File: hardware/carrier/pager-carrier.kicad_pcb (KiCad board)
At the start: 2 copper layers, 85 x 52 mm, 109 parts, among them J1 USB4235, J2 BATTERY, J3 PANEL, J4 CARDKB, J6 MSG_LED, J7 HAPTIC, M1 Walter, Q1 DMG2305UX-7, Q2 UMH3N, Q4 2N7002, SW1 JS102011SAQN, SW2 SKQGAFE010, U1 BQ25185DLHR, U10 MAX17048G+T10, U3 TPS62840DLCR, U4 TPS22917DBV, U5 CP2102N-A02-GQFN24, U6 SN74LVC2G126DCUR, U7 LIS2DW12TR, U9 DRV2605LDGSR

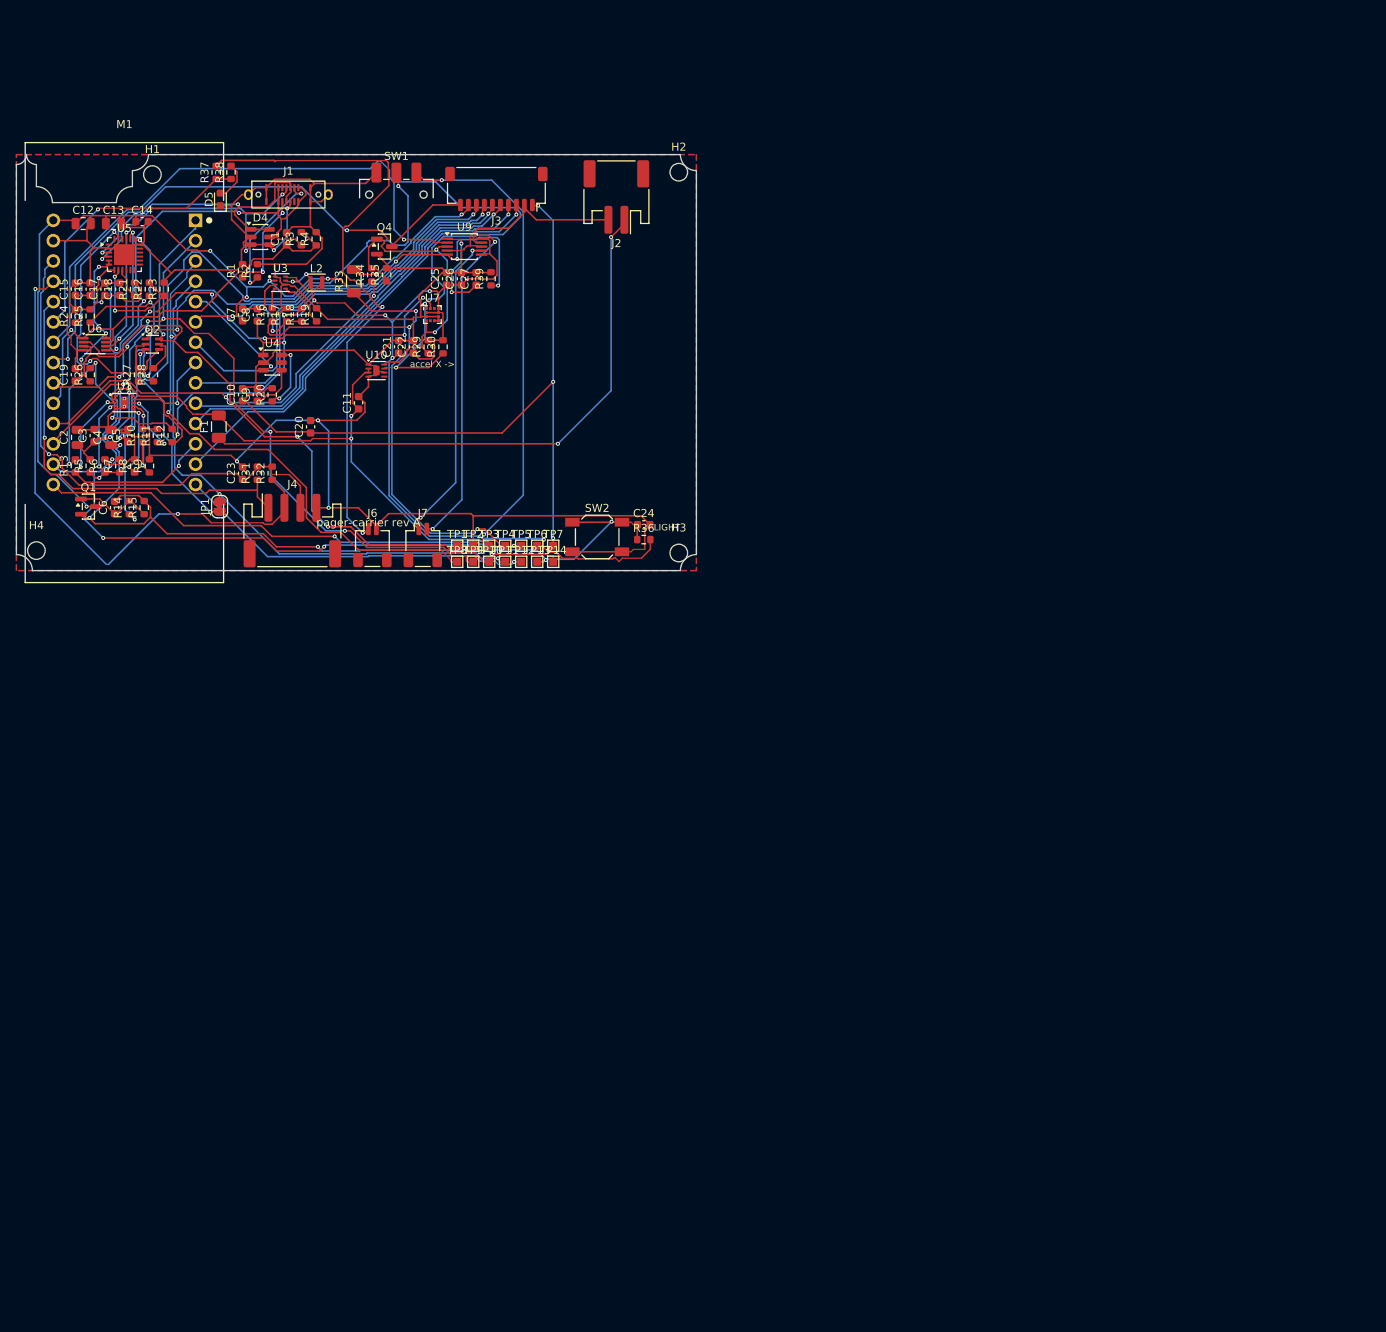
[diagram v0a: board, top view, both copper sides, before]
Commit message: Move sheets property to top level
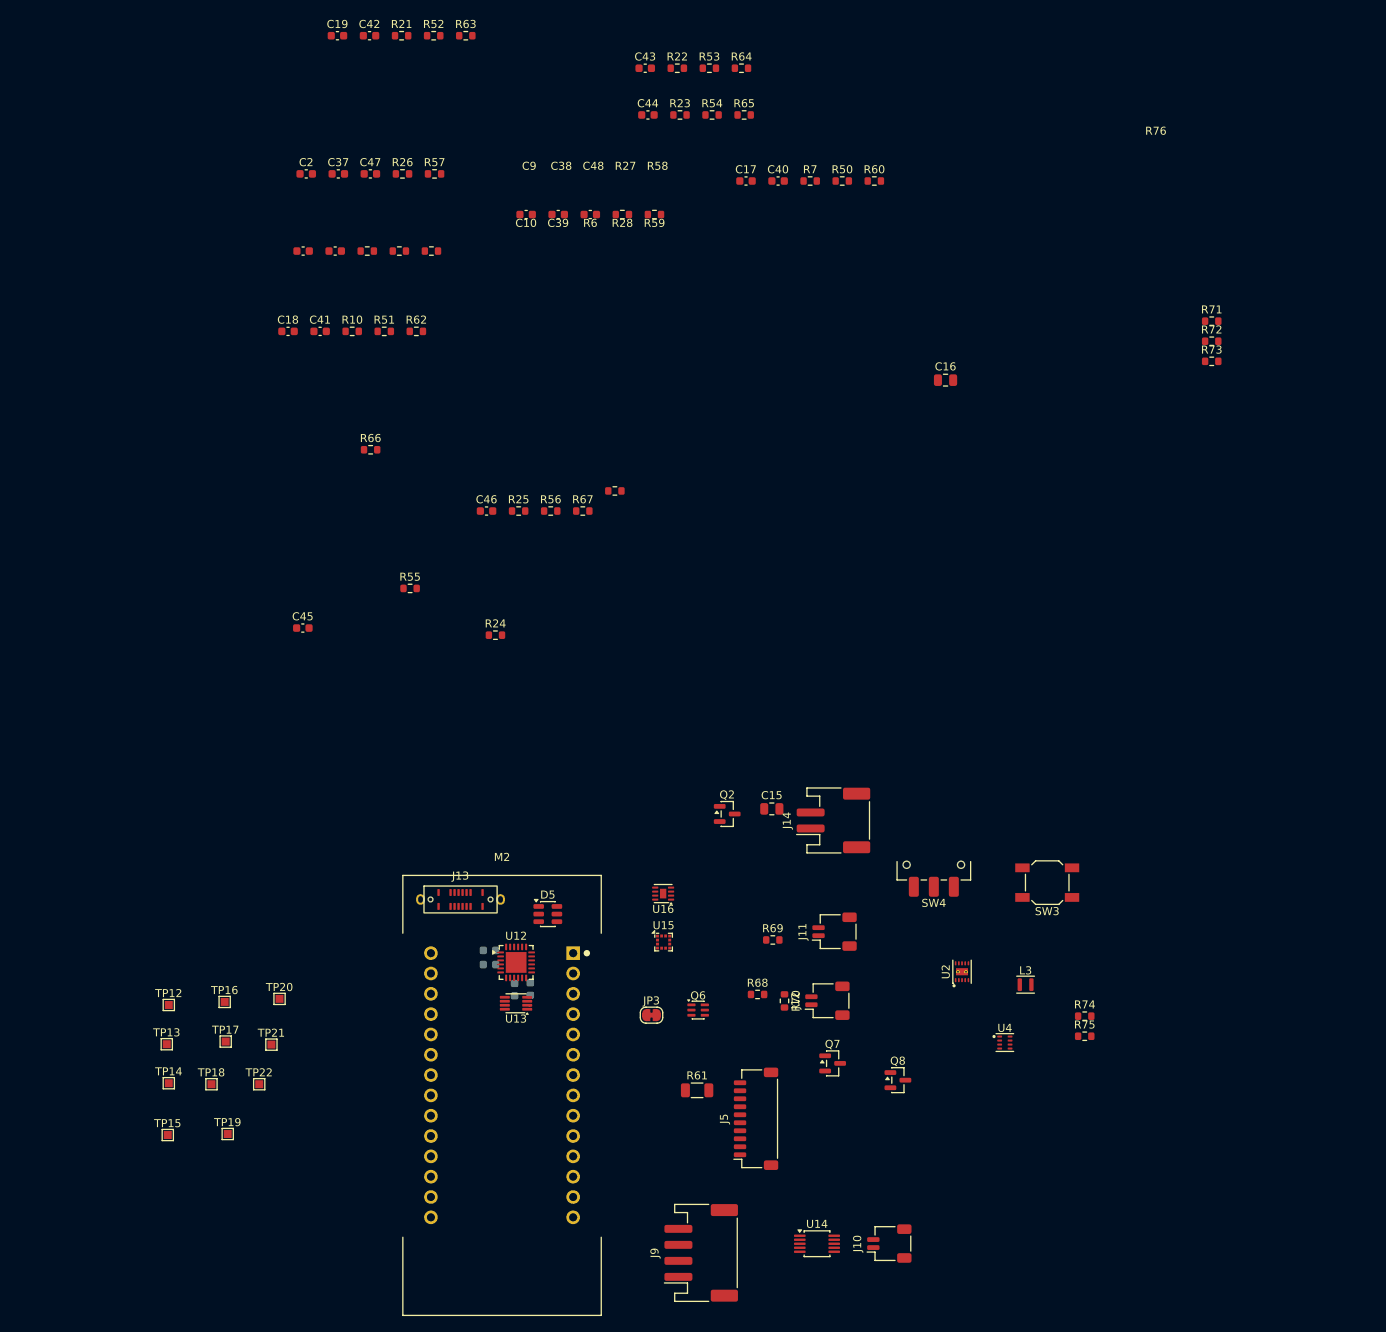
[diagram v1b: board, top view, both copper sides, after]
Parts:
- removed C1, C11, C21, C24, C26: 100nF, Capacitor_SMD:C_0603_1608Metric
- removed C12, C13: 100uF, Capacitor_SMD:C_0805_2012Metric
- removed C14, C20, C22, C23, C5, C7, C8: 10uF, Capacitor_SMD:C_0603_1608Metric
- removed C25, C27: 1uF, Capacitor_SMD:C_0603_1608Metric
- removed C3: 1uF/25V, Capacitor_SMD:C_0603_1608Metric
- removed C4: 22uF, Capacitor_SMD:C_0805_2012Metric
- removed C6: 22nF, Capacitor_SMD:C_0603_1608Metric
- removed D4: USBLC6-2SC6, Package_TO_SOT_SMD:SOT-23-6
- removed F1: 2A PTC, Fuse:Fuse_1206_3216Metric
- removed H1, H2, H3, H4: M2, MountingHole:MountingHole_2.2mm_M2
- removed J1: USB4235, pager-carrier:USB_C_Receptacle_GCT_USB4235_Vertical
- removed J2: BATTERY, Connector_JST:JST_PH_S2B-PH-SM4-TB_1x02-1MP_P2.00mm_Horizontal
- removed J3: PANEL, Connector_JST:JST_SH_SM10B-SRSS-TB_1x10-1MP_P1.00mm_Horizontal
- removed J4: CARDKB, Connector_JST:JST_PH_S4B-PH-SM4-TB_1x04-1MP_P2.00mm_Horizontal
- removed J6: MSG_LED, Connector_JST:JST_SH_SM02B-SRSS-TB_1x02-1MP_P1.00mm_Horizontal
- removed J7: HAPTIC, Connector_JST:JST_SH_SM02B-SRSS-TB_1x02-1MP_P1.00mm_Horizontal
- removed JP1: auto-boot, Jumper:SolderJumper-2_P1.3mm_Bridged_RoundedPad1.0x1.5mm
- removed L2: 2.2uH, Inductor_SMD:L_Murata_DFE201610P
- removed M1: Walter, pager-carrier:Walter_Module_2x14_THT
- removed Q1: DMG2305UX-7, Package_TO_SOT_SMD:SOT-23
- removed Q4: 2N7002, Package_TO_SOT_SMD:SOT-23
- removed R1, R2: 5.1k, Resistor_SMD:R_0603_1608Metric
- removed R11: 604R, Resistor_SMD:R_0603_1608Metric
- removed R12, R13, R14, R8: 10k, Resistor_SMD:R_0603_1608Metric
- removed R15: 2.2M, Resistor_SMD:R_0603_1608Metric
- removed R16, R35, R36, R39, R4: 100k, Resistor_SMD:R_0603_1608Metric
- removed R17, R18, R20, R5: 0R, Resistor_SMD:R_0603_1608Metric
- removed R19: 267k, Resistor_SMD:R_0603_1608Metric
- removed R29, R30, R31, R32: 4.7k, Resistor_SMD:R_0603_1608Metric
- removed R3: 56k, Resistor_SMD:R_0603_1608Metric
- removed R33: 33R, Resistor_SMD:R_1206_3216Metric
- removed R34: 100R, Resistor_SMD:R_0603_1608Metric
- removed R37: 330R, Resistor_SMD:R_0603_1608Metric
- removed R38: 1k, Resistor_SMD:R_0603_1608Metric
- removed R9: 18k, Resistor_SMD:R_0603_1608Metric
- removed SW1: JS102011SAQN, Button_Switch_SMD:SW_SPDT_CK_JS102011SAQN
- removed SW2: SKQGAFE010, Button_Switch_SMD:SW_SPST_SKQG_WithoutStem
- removed TP1, TP2: GND, TestPoint:TestPoint_Pad_1.0x1.0mm
- removed TP10: ESP_EN, TestPoint:TestPoint_Pad_1.0x1.0mm
- removed TP11: KBD_PWR_N, TestPoint:TestPoint_Pad_1.0x1.0mm
- removed TP3: SYS, TestPoint:TestPoint_Pad_1.0x1.0mm
- removed TP4: SYS_SW, TestPoint:TestPoint_Pad_1.0x1.0mm
- removed TP5: VBAT, TestPoint:TestPoint_Pad_1.0x1.0mm
- removed TP6: 3V3, TestPoint:TestPoint_Pad_1.0x1.0mm
- removed TP7: 3V3_EPD, TestPoint:TestPoint_Pad_1.0x1.0mm
- removed TP8: ESP_TX0, TestPoint:TestPoint_Pad_1.0x1.0mm
- removed TP9: ESP_RX0, TestPoint:TestPoint_Pad_1.0x1.0mm
- removed U1: BQ25185DLHR, pager-carrier:BQ25185_WSON-10_DLH0010A_2.2x2mm_P0.4mm_EP0.9x1.5mm
- removed U10: MAX17048G+T10, Package_DFN_QFN:TDFN-8-1EP_2x2mm_P0.5mm_EP0.8x1.2mm
- removed U3: TPS62840DLCR, pager-carrier:TPS62840_VSON-HR-8_DLC0008B_1.5x2mm_P0.5mm
- removed U5: CP2102N-A02-GQFN24, Package_DFN_QFN:QFN-24-1EP_4x4mm_P0.5mm_EP2.6x2.6mm
- removed U6: SN74LVC2G126DCUR, Package_SO:VSSOP-8_2.3x2mm_P0.5mm
- removed U7: LIS2DW12TR, Package_LGA:LGA-12_2x2mm_P0.5mm
- removed U9: DRV2605LDGSR, Package_SO:TSSOP-10_3x3mm_P0.5mm
- added C33: 4.7uF, Capacitor_SMD:C_0603_1608Metric, B.Cu at (59.1, 99.5)
- added C34: 100nF, Capacitor_SMD:C_0603_1608Metric, B.Cu at (59.1, 101.2)
- added C35: 100nF, Capacitor_SMD:C_0603_1608Metric, B.Cu at (62.3, 104.4)
- added C36: 4.7uF, Capacitor_SMD:C_0603_1608Metric, B.Cu at (64.2, 104.3)
- added C37: 100nF, Capacitor_SMD:C_0603_1608Metric, F.Cu at (40.2, 2.41)
- added C38: 10uF, Capacitor_SMD:C_0603_1608Metric, F.Cu at (67.7, 7.49)
- added C39: 100nF, Capacitor_SMD:C_0603_1608Metric, F.Cu at (39.9, 12.1)
- added C40: 10uF, Capacitor_SMD:C_0603_1608Metric, F.Cu at (95.2, 3.30)
- added C41: 1uF, Capacitor_SMD:C_0603_1608Metric, F.Cu at (38.0, 22.1)
- added C42: 100nF, Capacitor_SMD:C_0603_1608Metric, F.Cu at (44.1, -14.9)
- added C43: 10uF, Capacitor_SMD:C_0603_1608Metric, F.Cu at (78.6, -10.8)
- added C44: 1uF, Capacitor_SMD:C_0603_1608Metric, F.Cu at (78.9, -4.95)
- added C45: 100nF, Capacitor_SMD:C_0603_1608Metric, F.Cu at (35.8, 59.2)
- added C46: 100nF, Capacitor_SMD:C_0603_1608Metric, F.Cu at (58.8, 44.6)
- added C47: 10uF, Capacitor_SMD:C_0603_1608Metric, F.Cu at (44.2, 2.41)
- added C48: 10uF, Capacitor_SMD:C_0603_1608Metric, F.Cu at (71.7, 7.49)
- added J10: HAPTIC, Connector_JST:JST_SH_SM02B-SRSS-TB_1x02-1MP_P1.00mm_Horizontal, F.Cu at (109.1, 136.1)
- added J11: EXT_LED, Connector_JST:JST_SH_SM02B-SRSS-TB_1x02-1MP_P1.00mm_Horizontal, F.Cu at (102.3, 97.1)
- added J12: PIEZ, Connector_JST:JST_SH_SM02B-SRSS-TB_1x02-1MP_P1.00mm_Horizontal, F.Cu at (101.4, 105.8)
- added J13: USB4235, pager-carrier:USB_C_Receptacle_GCT_USB4235_Vertical, F.Cu at (55.5, 93.1)
- added J14: BATTERY, Connector_JST:JST_PH_S2B-PH-SM4-TB_1x02-1MP_P2.00mm_Horizontal, F.Cu at (102.1, 83.2)
- added J5: PANEL, Connector_JST:JST_SH_SM10B-SRSS-TB_1x10-1MP_P1.00mm_Horizontal, F.Cu at (92.5, 120.5)
- added J9: CARDKB, Connector_JST:JST_PH_S4B-PH-SM4-TB_1x04-1MP_P2.00mm_Horizontal, F.Cu at (85.6, 137.3)
- added JP3: auto-boot, Jumper:SolderJumper-2_P1.3mm_Bridged_RoundedPad1.0x1.5mm, F.Cu at (79.4, 107.6)
- added L3: 2.2uH, Inductor_SMD:L_Murata_DFE201610P, F.Cu at (126.1, 103.8)
- added M2: Walter, pager-carrier:Walter_Module_2x14_THT, F.Cu at (60.7, 116.3)
- added Q6: UMH3N, Package_TO_SOT_SMD:SOT-363_SC-70-6, F.Cu at (85.2, 106.9)
- added Q7: AO3400A, Package_TO_SOT_SMD:SOT-23, F.Cu at (102.0, 113.6)
- added Q8: MMBT3904, Package_TO_SOT_SMD:SOT-23, F.Cu at (110.2, 115.7)
- added R50: 22.1k, Resistor_SMD:R_0603_1608Metric, F.Cu at (103.2, 3.30)
- added R51: 47.5k, Resistor_SMD:R_0603_1608Metric, F.Cu at (46.0, 22.1)
- added R52: 1k, Resistor_SMD:R_0603_1608Metric, F.Cu at (52.2, -14.9)
- added R53: 100k, Resistor_SMD:R_0603_1608Metric, F.Cu at (86.6, -10.8)
- added R54: 100k, Resistor_SMD:R_0603_1608Metric, F.Cu at (87.0, -4.95)
- added R55: 100k, Resistor_SMD:R_0603_1608Metric, F.Cu at (49.2, 54.2)
- added R56: 10k, Resistor_SMD:R_0603_1608Metric, F.Cu at (66.8, 44.6)
- added R57: 10k, Resistor_SMD:R_0603_1608Metric, F.Cu at (52.3, 2.41)
- added R58: 1k, Resistor_SMD:R_0603_1608Metric, F.Cu at (79.8, 7.49)
- added R59: 100k, Resistor_SMD:R_0603_1608Metric, F.Cu at (51.9, 12.1)
- added R60: 15R, Resistor_SMD:R_0603_1608Metric, F.Cu at (107.2, 3.30)
- added R61: 0R, Resistor_SMD:R_1206_3216Metric, F.Cu at (85.1, 117.0)
- added R62: 10k, Resistor_SMD:R_0603_1608Metric, F.Cu at (50.0, 22.1)
- added R63: 4.7k, Resistor_SMD:R_0603_1608Metric, F.Cu at (56.2, -14.9)
- added R64: 4.7k, Resistor_SMD:R_0603_1608Metric, F.Cu at (90.6, -10.8)
- added R65: 4.7k, Resistor_SMD:R_0603_1608Metric, F.Cu at (91.0, -4.95)
- added R66: 4.7k, Resistor_SMD:R_0603_1608Metric, F.Cu at (44.3, 36.9)
- added R67: 220R, Resistor_SMD:R_0603_1608Metric, F.Cu at (70.8, 44.6)
- added R68: 220R, Resistor_SMD:R_0603_1608Metric, F.Cu at (92.6, 105.0)
- added R69: 330R, Resistor_SMD:R_0603_1608Metric, F.Cu at (94.6, 98.2)
- added R70: 1M, Resistor_SMD:R_0603_1608Metric, F.Cu at (96.0, 105.8)
- added R71: 56k, Resistor_SMD:R_0603_1608Metric, F.Cu at (149.4, 20.8)
- added R72: 100k, Resistor_SMD:R_0603_1608Metric, F.Cu at (149.4, 23.3)
- added R73: 0R, Resistor_SMD:R_0603_1608Metric, F.Cu at (149.4, 25.8)
- added R74: 0R, Resistor_SMD:R_0603_1608Metric, F.Cu at (133.5, 107.7)
- added R75: 100k, Resistor_SMD:R_0603_1608Metric, F.Cu at (133.5, 110.2)
- added R76: 267k, Resistor_SMD:R_0603_1608Metric, F.Cu at (74.8, 42.0)
- added SW3: SKQGAFE010, Button_Switch_SMD:SW_SPST_SKQG_WithoutStem, F.Cu at (128.9, 91.0)
- added SW4: JS102011SAQN, Button_Switch_SMD:SW_SPDT_CK_JS102011SAQN, F.Cu at (114.7, 88.8)
- added TP15: FL_BTN, TestPoint:TestPoint_Pad_1.0x1.0mm, F.Cu at (18.9, 122.6)
- added TP16: 3V3_AWK, TestPoint:TestPoint_Pad_1.0x1.0mm, F.Cu at (26.0, 105.9)
- added TP17: GND, TestPoint:TestPoint_Pad_1.0x1.0mm, F.Cu at (26.2, 110.9)
- added TP18: VBUS, TestPoint:TestPoint_Pad_1.0x1.0mm, F.Cu at (24.4, 116.2)
- added TP19: SYS, TestPoint:TestPoint_Pad_1.0x1.0mm, F.Cu at (26.4, 122.4)
- added TP20: SYS_SW, TestPoint:TestPoint_Pad_1.0x1.0mm, F.Cu at (32.9, 105.5)
- added TP21: VBAT, TestPoint:TestPoint_Pad_1.0x1.0mm, F.Cu at (31.9, 111.3)
- added TP22: 3V3, TestPoint:TestPoint_Pad_1.0x1.0mm, F.Cu at (30.4, 116.2)
- added U12: CP2102N-A02-GQFN24, Package_DFN_QFN:QFN-24-1EP_4x4mm_P0.5mm_EP2.6x2.6mm, F.Cu at (62.5, 101.0)
- added U13: SN74LVC2G126DCUR, Package_SO:VSSOP-8_2.3x2mm_P0.5mm, F.Cu at (62.5, 106.1)
- added U14: DRV2605LDGSR, Package_SO:TSSOP-10_3x3mm_P0.5mm, F.Cu at (100.1, 136.1)
- added U15: LIS2DW12TR, Package_LGA:LGA-12_2x2mm_P0.5mm, F.Cu at (80.9, 98.4)
- added U16: MAX17048G+T10, Package_DFN_QFN:TDFN-8-1EP_2x2mm_P0.5mm_EP0.8x1.2mm, F.Cu at (80.8, 92.4)
- added U2: BQ25185DLHR, pager-carrier:BQ25185_WSON-10_DLH0010A_2.2x2mm_P0.4mm_EP0.9x1.5mm, F.Cu at (118.2, 102.1)
- C10: value 1uF -> 22nF
- C15: value 4.7uF -> 100uF; footprint Capacitor_SMD:C_0603_1608Metric -> Capacitor_SMD:C_0805_2012Metric
- C16: value 100nF -> 100uF; footprint Capacitor_SMD:C_0603_1608Metric -> Capacitor_SMD:C_0805_2012Metric
- C17: value 4.7uF -> 10uF
- C18, C19: value 100nF -> 10uF
- C2: value 10uF/25V -> 100nF; footprint Capacitor_SMD:C_0805_2012Metric -> Capacitor_SMD:C_0603_1608Metric
- C9: value 1nF -> 1uF/25V
- D5: value RED -> USBLC6-2SC6; footprint LED_SMD:LED_0603_1608Metric -> Package_TO_SOT_SMD:SOT-23-6
- Q2: value UMH3N -> AO3401A; footprint Package_TO_SOT_SMD:SOT-363_SC-70-6 -> Package_TO_SOT_SMD:SOT-23
- R10: value 13k -> 10k
- R21: value 1k -> 0R
- R22: value 22.1k -> 18k
- R23: value 47.5k -> 10k
- R24: value 100k -> 604R
- R25: value 100k -> 10k
- R27: value 10k -> 5.1k
- R28: value 10k -> 2.2M
- R7: value 0R -> 5.1k
- TP12: value TP_IO1 -> AWK_EN_N
- TP13: value FL_BTN -> TP_IO1
- U4: value TPS22917DBV -> TPS62840DLCR; footprint Package_TO_SOT_SMD:SOT-23-6 -> pager-carrier:TPS62840_VSON-HR-8_DLC0008B_1.5x2mm_P0.5mm
- moved U4 124.9 mm to (123.6, 111.0)
- moved C15 108.6 mm to (94.4, 81.8), turned to 0 degrees
- moved C16 107.5 mm to (116.1, 28.2), turned to 0 degrees
- moved D5 98.3 mm to (66.4, 94.9), turned to 0 degrees
- moved R7 93.4 mm to (99.2, 3.30), turned to 0 degrees
- moved Q2 92.8 mm to (88.9, 82.4)
- moved C17 81.3 mm to (91.2, 3.30), turned to 0 degrees
- moved TP14 81.0 mm to (19.1, 116.1)
- moved TP13 76.0 mm to (18.8, 111.2)
- moved R22 71.5 mm to (82.6, -10.8), turned to 0 degrees
- moved TP12 70.8 mm to (19.1, 106.3)
- moved R23 68.1 mm to (83.0, -4.95), turned to 0 degrees
- moved R24 65.9 mm to (59.9, 60.1), turned to 0 degrees
- moved R27 63.7 mm to (75.7, 7.49), turned to 0 degrees
- moved R25 58.8 mm to (62.8, 44.6), turned to 0 degrees
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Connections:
- C10 pad 1: 3V3_EPD -> Net-(Q2-G)
- C10 pad 2: GND -> SYS
- C15 pad 1: VBUS -> SYS_SW
- C16 pad 1: VBUS -> SYS_SW
- C17 pad 1: BRG_VDD -> SYS_SW
- C18 pad 1: BRG_VDD -> SYS
- C19 pad 1: BRG_VDD -> VBAT
- C2 pad 1: CHG_IN -> VBUS_DET
- C9 pad 1: EPD_CT -> Net-(U2-IN)
- D5 pad 1: GND -> Net-(D5-I/O1-Pad1)
- D5 pad 2: LED_D5 -> GND
- Q2 pad 1: BRG_RTS -> Net-(Q2-G)
- Q2 pad 2: RST_B1 -> SYS
- Q2 pad 3: IO0_RST -> SYS_SW
- R10 pad 1: CHG_ILIM -> Net-(U2-TS/MR)
- R21 pad 1: BRG_RST -> 3V3
- R21 pad 2: BRG_VDD -> Net-(J5-Pin_1)
- R22 pad 1: VBUS -> Net-(U2-ILIM/VSET)
- R22 pad 2: BRG_VBUS_SNS -> GND
- R23 pad 1: BRG_VBUS_SNS -> 3V3
- R23 pad 2: GND -> CHG_STAT1
- R24 pad 1: BRG_DTR -> Net-(U2-ISET)
- R25 pad 1: BRG_RTS -> 3V3
- R25 pad 2: GND -> CHG_STAT2
- R26 pad 1: ESP_RX0 -> Net-(SW4-B)
- R26 pad 2: 3V3 -> Net-(Q2-G)
- R27 pad 1: BRG_DTR -> Net-(J13-CC1)
- R27 pad 2: RST_B1 -> GND
- R28 pad 1: BRG_RTS -> Net-(Q2-G)
- R28 pad 2: RST_B2 -> SYS
- R6 pad 1: CHG_CE -> VBUS
- R6 pad 2: GND -> Net-(U2-IN)
- R7 pad 1: CHG_CE -> Net-(J13-CC2)
- R7 pad 2: TP_IO5 -> GND
- TP12 pad 1: TP_IO1 -> /Core/AWK_EN_N
- TP13 pad 1: FL_BTN -> /Core/TP_IO1
- TP14 pad 1: TP_IO5 -> /Core/TP_IO5
- U4 pad 1: 3V3 -> GND
- U4 pad 2: GND -> SYS_SW
- U4 pad 3: EPD_ENA -> Net-(U4-MODE)
- U4 pad 4: EPD_CT -> Net-(U4-EN)
- U4 pad 5: unconnected-(U4-QOD-Pad5) -> Net-(U4-VSET)
- U4 pad 6: EPD_SW_OUT -> GND
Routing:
- net GND: track 382.6 -> 0.00 mm, vias 3 -> 0
- net 3V3: track 190.4 -> 0.00 mm, vias 11 -> 0
- net SYS_SW: track 163.0 -> 0.00 mm, vias 8 -> 0
- net SYS: track 141.6 -> 0.00 mm, vias 7 -> 0
- net ACC_SCL: track 129.5 -> 0.00 mm, vias 3 -> 0
- net ACC_SDA: track 93.2 -> 0.00 mm, vias 4 -> 0
- net 3V3_EPD: track 91.6 -> 0.00 mm, vias 3 -> 0
- net VBUS: track 90.3 -> 0.00 mm, vias 4 -> 0
- net SW_COM: track 89.4 -> 0.00 mm, vias 2 -> 0
- net FL_BTN: track 87.1 -> 0.00 mm, vias 3 -> 0
- net ESP_RX0: track 87.1 -> 0.00 mm, vias 5 -> 0
- net ESP_TX0: track 83.4 -> 0.00 mm, vias 2 -> 0
- net VBAT: track 82.3 -> 0.00 mm, vias 5 -> 0
- net HAPTIC_EN: track 80.4 -> 0.00 mm, vias 6 -> 0
- net TP_IO5: track 77.6 -> 0.00 mm, vias 4 -> 0
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- removed copper zone on B.Cu, net GND
- removed copper zone on F.Cu, net GND
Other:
- board outline removed
- board text removed: "LIGHT"
- board text removed: "SIM loads from this edge (Walter beneath)"
- board text removed: "WALTER UNDERNEATH, header side up"
- board text removed: "accel X ->"
- board text removed: "antenna pigtails"
- board text removed: "glass 79 x 36.7 (GDEY029T94)"
- board text removed: "pager-carrier rev A"
- board text removed: "panel board here"

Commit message: Attempt to layout the PCB
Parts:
- removed C33, C36: 4.7uF, Capacitor_SMD:C_0603_1608Metric
- removed C34, C35, C37, C39, C42, C45, C46: 100nF, Capacitor_SMD:C_0603_1608Metric
- removed C38, C40, C43, C47, C48: 10uF, Capacitor_SMD:C_0603_1608Metric
- removed C41, C44: 1uF, Capacitor_SMD:C_0603_1608Metric
- removed D5: USBLC6-2SC6, Package_TO_SOT_SMD:SOT-23-6
- removed J10: HAPTIC, Connector_JST:JST_SH_SM02B-SRSS-TB_1x02-1MP_P1.00mm_Horizontal
- removed J11: EXT_LED, Connector_JST:JST_SH_SM02B-SRSS-TB_1x02-1MP_P1.00mm_Horizontal
- removed J12: PIEZ, Connector_JST:JST_SH_SM02B-SRSS-TB_1x02-1MP_P1.00mm_Horizontal
- removed J13: USB4235, pager-carrier:USB_C_Receptacle_GCT_USB4235_Vertical
- removed J14: BATTERY, Connector_JST:JST_PH_S2B-PH-SM4-TB_1x02-1MP_P2.00mm_Horizontal
- removed J9: CARDKB, Connector_JST:JST_PH_S4B-PH-SM4-TB_1x04-1MP_P2.00mm_Horizontal
- removed JP3: auto-boot, Jumper:SolderJumper-2_P1.3mm_Bridged_RoundedPad1.0x1.5mm
- removed L3: 2.2uH, Inductor_SMD:L_Murata_DFE201610P
- removed M2: Walter, pager-carrier:Walter_Module_2x14_THT
- removed Q6: UMH3N, Package_TO_SOT_SMD:SOT-363_SC-70-6
- removed Q7: AO3400A, Package_TO_SOT_SMD:SOT-23
- removed Q8: MMBT3904, Package_TO_SOT_SMD:SOT-23
- removed R50: 22.1k, Resistor_SMD:R_0603_1608Metric
- removed R51: 47.5k, Resistor_SMD:R_0603_1608Metric
- removed R52, R58: 1k, Resistor_SMD:R_0603_1608Metric
- removed R53, R54, R55, R59, R72, R75: 100k, Resistor_SMD:R_0603_1608Metric
- removed R56, R57, R62: 10k, Resistor_SMD:R_0603_1608Metric
- removed R60: 15R, Resistor_SMD:R_0603_1608Metric
- removed R61: 0R, Resistor_SMD:R_1206_3216Metric
- removed R63, R64, R65, R66: 4.7k, Resistor_SMD:R_0603_1608Metric
- removed R67, R68: 220R, Resistor_SMD:R_0603_1608Metric
- removed R69: 330R, Resistor_SMD:R_0603_1608Metric
- removed R70: 1M, Resistor_SMD:R_0603_1608Metric
- removed R71: 56k, Resistor_SMD:R_0603_1608Metric
- removed R73, R74: 0R, Resistor_SMD:R_0603_1608Metric
- removed R76: 267k, Resistor_SMD:R_0603_1608Metric
- removed SW3: SKQGAFE010, Button_Switch_SMD:SW_SPST_SKQG_WithoutStem
- removed SW4: JS102011SAQN, Button_Switch_SMD:SW_SPDT_CK_JS102011SAQN
- removed TP12: AWK_EN_N, TestPoint:TestPoint_Pad_1.0x1.0mm
- removed TP13: TP_IO1, TestPoint:TestPoint_Pad_1.0x1.0mm
- removed TP14: TP_IO5, TestPoint:TestPoint_Pad_1.0x1.0mm
- removed TP15: FL_BTN, TestPoint:TestPoint_Pad_1.0x1.0mm
- removed TP16: 3V3_AWK, TestPoint:TestPoint_Pad_1.0x1.0mm
- removed TP17: GND, TestPoint:TestPoint_Pad_1.0x1.0mm
- removed TP18: VBUS, TestPoint:TestPoint_Pad_1.0x1.0mm
- removed TP19: SYS, TestPoint:TestPoint_Pad_1.0x1.0mm
- removed TP20: SYS_SW, TestPoint:TestPoint_Pad_1.0x1.0mm
- removed TP21: VBAT, TestPoint:TestPoint_Pad_1.0x1.0mm
- removed TP22: 3V3, TestPoint:TestPoint_Pad_1.0x1.0mm
- removed U12: CP2102N-A02-GQFN24, Package_DFN_QFN:QFN-24-1EP_4x4mm_P0.5mm_EP2.6x2.6mm
- removed U13: SN74LVC2G126DCUR, Package_SO:VSSOP-8_2.3x2mm_P0.5mm
- removed U14: DRV2605LDGSR, Package_SO:TSSOP-10_3x3mm_P0.5mm
- removed U15: LIS2DW12TR, Package_LGA:LGA-12_2x2mm_P0.5mm
- removed U16: MAX17048G+T10, Package_DFN_QFN:TDFN-8-1EP_2x2mm_P0.5mm_EP0.8x1.2mm
- added C1: 4.7uF, Capacitor_SMD:C_0603_1608Metric, F.Cu at (82.2, 63.2)
- added C11: 1uF, Capacitor_SMD:C_0402_1005Metric, F.Cu at (114.9, 76.0)
- added C12: 100nF, Capacitor_SMD:C_0402_1005Metric, F.Cu at (83.7, 83.7)
- added C13: 1uF/25V, Capacitor_SMD:C_0603_1608Metric, F.Cu at (121.6, 33.0)
- added C14: 22nF, Capacitor_SMD:C_0402_1005Metric, F.Cu at (115.2, 24.4)
- added C3: 100nF, Capacitor_SMD:C_0402_1005Metric, F.Cu at (85.1, 61.3)
- added C4: 4.7uF, Capacitor_SMD:C_0402_1005Metric, F.Cu at (86.1, 61.2)
- added C5: 100nF, Capacitor_SMD:C_0402_1005Metric, F.Cu at (74.8, 100.7)
- added C6: 100uF, Capacitor_SMD:C_0805_2012Metric, F.Cu at (75.2, 68.5)
- added C7: 100uF, Capacitor_SMD:C_0805_2012Metric, F.Cu at (73.2, 68.5)
- added C8: 10uF, Capacitor_SMD:C_0603_1608Metric, F.Cu at (101.0, 100.8)
- added D1: USBLC6-2P6, Package_TO_SOT_SMD:SOT-666, F.Cu at (105.9, 65.8)
- added J1: PANEL, Connector_JST:JST_SH_SM10B-SRSS-TB_1x10-1MP_P1.00mm_Horizontal, F.Cu at (109.9, 96.4)
- added J2: CARDKB, Connector_JST:JST_SH_SM04B-SRSS-TB_1x04-1MP_P1.00mm_Horizontal, F.Cu at (89.3, 81.0)
- added J3: HAPTIC, Connector_JST:JST_SH_SM02B-SRSS-TB_1x02-1MP_P1.00mm_Horizontal, F.Cu at (124.2, 78.5)
- added J4: EXT_LED, Connector_JST:JST_SH_SM02B-SRSS-TB_1x02-1MP_P1.00mm_Horizontal, F.Cu at (123.8, 94.9)
- added J6: USB4235, pager-carrier:USB_C_Receptacle_GCT_USB4235_Vertical, F.Cu at (107.7, 62.0)
- added J7: BATTERY, Connector_JST:JST_PH_S2B-PH-SM4-TB_1x02-1MP_P2.00mm_Horizontal, F.Cu at (125.0, 64.3)
- added JP1: auto-boot, Jumper:SolderJumper-2_P1.3mm_Bridged_RoundedPad1.0x1.5mm, F.Cu at (91.8, 68.7)
- added L1: 2.2uH, Inductor_SMD:L_Murata_DFE201610P, F.Cu at (109.8, 70.4)
- added M1: Walter, pager-carrier:Walter_Module_2x14_THT, F.Cu at (86.7, 83.4)
- added Q1: UMH3N, Package_TO_SOT_SMD:SOT-363_SC-70-6, F.Cu at (90.9, 72.4)
- added Q3: MMST3904, Package_TO_SOT_SMD:SOT-323_SC-70, F.Cu at (99.9, 89.7)
- added Q4: AO3401A, Package_TO_SOT_SMD:SOT-23, F.Cu at (118.8, 27.6)
- added R1: 22.1k, Resistor_SMD:R_0402_1005Metric, F.Cu at (82.3, 65.5)
- added R11: 0R, Resistor_SMD:R_0402_1005Metric, F.Cu at (104.4, 100.8)
- added R12: 15R, Resistor_SMD:R_0603_1608Metric, F.Cu at (99.9, 92.6)
- added R13: 0R, Resistor_SMD:R_0402_1005Metric, F.Cu at (105.1, 88.4)
- added R14: 10k, Resistor_SMD:R_0402_1005Metric, F.Cu at (98.6, 62.1)
- added R15: 4.7k, Resistor_SMD:R_0402_1005Metric, F.Cu at (89.6, 76.3)
- added R16: 4.7k, Resistor_SMD:R_0402_1005Metric, F.Cu at (90.8, 76.3)
- added R17: 4.7k, Resistor_SMD:R_0402_1005Metric, F.Cu at (74.8, 84.7)
- added R18: 4.7k, Resistor_SMD:R_0402_1005Metric, F.Cu at (74.8, 82.2)
- added R19: 220R, Resistor_SMD:R_0402_1005Metric, F.Cu at (119.6, 87.6)
- added R2: 47.5k, Resistor_SMD:R_0402_1005Metric, F.Cu at (82.3, 66.7)
- added R20: 220R, Resistor_SMD:R_0402_1005Metric, F.Cu at (119.6, 86.6)
- added R29: 5.1k, Resistor_SMD:R_0402_1005Metric, F.Cu at (112.1, 64.9)
- added R3: 1k, Resistor_SMD:R_0402_1005Metric, F.Cu at (82.3, 67.7)
- added R30: 10k, Resistor_SMD:R_0402_1005Metric, F.Cu at (111.2, 32.2)
- added R31: 5.1k, Resistor_SMD:R_0402_1005Metric, F.Cu at (112.5, 66.9)
- added R32: 2.2M, Resistor_SMD:R_0402_1005Metric, F.Cu at (111.2, 36.1)
- added R33: 56k, Resistor_SMD:R_0402_1005Metric, F.Cu at (81.8, 76.6)
- added R34: 100k, Resistor_SMD:R_0402_1005Metric, F.Cu at (84.7, 72.9)
- added R35: 0R, Resistor_SMD:R_0402_1005Metric, F.Cu at (103.8, 73.5)
- added R36: 0R, Resistor_SMD:R_0402_1005Metric, F.Cu at (103.8, 72.5)
- added R37: 100k, Resistor_SMD:R_0402_1005Metric, F.Cu at (103.8, 74.5)
- added R38: 267k, Resistor_SMD:R_0402_1005Metric, F.Cu at (109.2, 72.5)
- added R4: 100k, Resistor_SMD:R_0402_1005Metric, F.Cu at (90.1, 67.8)
- added R5: 100k, Resistor_SMD:R_0402_1005Metric, F.Cu at (74.8, 99.6)
- added R8: 10k, Resistor_SMD:R_0402_1005Metric, F.Cu at (88.5, 70.2)
- added R9: 1k, Resistor_SMD:R_0402_1005Metric, F.Cu at (103.9, 88.4)
- added SW1: SKQGAFE010, Button_Switch_SMD:SW_SPST_SKQG_WithoutStem, F.Cu at (80.3, 52.1)
- added SW2: JS102011SAQN, Button_Switch_SMD:SW_SPDT_CK_JS102011SAQN, F.Cu at (115.7, 43.0)
- added TP1: AWK_EN_N, TestPoint:TestPoint_Pad_1.0x1.0mm, F.Cu at (164.9, 25.1)
- added TP10: VBAT, TestPoint:TestPoint_Pad_1.0x1.0mm, F.Cu at (156.2, 28.2)
- added TP11: 3V3, TestPoint:TestPoint_Pad_1.0x1.0mm, F.Cu at (156.2, 31.2)
- added TP2: TP_IO1, TestPoint:TestPoint_Pad_1.0x1.0mm, F.Cu at (164.9, 28.2)
- added TP3: TP_IO5, TestPoint:TestPoint_Pad_1.0x1.0mm, F.Cu at (164.9, 31.2)
- added TP4: FL_BTN, TestPoint:TestPoint_Pad_1.0x1.0mm, F.Cu at (164.9, 34.3)
- added TP5: 3V3_AWK, TestPoint:TestPoint_Pad_1.0x1.0mm, F.Cu at (167.9, 25.1)
- added TP6: GND, TestPoint:TestPoint_Pad_1.0x1.0mm, F.Cu at (153.2, 28.2)
- added TP7: VBUS, TestPoint:TestPoint_Pad_1.0x1.0mm, F.Cu at (153.2, 31.2)
- added TP8: SYS, TestPoint:TestPoint_Pad_1.0x1.0mm, F.Cu at (153.2, 34.3)
- added TP9: SYS_SW, TestPoint:TestPoint_Pad_1.0x1.0mm, F.Cu at (156.2, 25.1)
- added U1: CP2102N-A02-GQFN24, Package_DFN_QFN:QFN-24-1EP_4x4mm_P0.5mm_EP2.6x2.6mm, F.Cu at (86.7, 65.4)
- added U3: DRV2605LDGSR, Package_SO:TSSOP-10_3x3mm_P0.5mm, F.Cu at (117.0, 78.5)
- added U5: BQ25185DLHR, pager-carrier:BQ25185_WSON-10_DLH0010A_2.2x2mm_P0.4mm_EP0.9x1.5mm, F.Cu at (123.6, 35.9)
- added U6: MAX17048G+T10, Package_DFN_QFN:TDFN-8-1EP_2x2mm_P0.5mm_EP0.8x1.2mm, F.Cu at (116.9, 68.4)
- added U7: TPS62840DLCR, pager-carrier:TPS62840_VSON-HR-8_DLC0008B_1.5x2mm_P0.5mm, F.Cu at (106.6, 71.8)
- C10: value 22nF -> 1uF; footprint Capacitor_SMD:C_0603_1608Metric -> Capacitor_SMD:C_0402_1005Metric
- C15, C16: value 100uF -> 10uF; footprint Capacitor_SMD:C_0805_2012Metric -> Capacitor_SMD:C_0402_1005Metric
- C17, C18: value 10uF -> 100nF; footprint Capacitor_SMD:C_0603_1608Metric -> Capacitor_SMD:C_0402_1005Metric
- C19, C2: footprint Capacitor_SMD:C_0603_1608Metric -> Capacitor_SMD:C_0402_1005Metric
- C9: value 1uF/25V -> 100nF; footprint Capacitor_SMD:C_0603_1608Metric -> Capacitor_SMD:C_0402_1005Metric
- J5: value PANEL -> PIEZ; footprint Connector_JST:JST_SH_SM10B-SRSS-TB_1x10-1MP_P1.00mm_Horizontal -> Connector_JST:JST_SH_SM02B-SRSS-TB_1x02-1MP_P1.00mm_Horizontal
- Q2: value AO3401A -> SI1308EDL; footprint Package_TO_SOT_SMD:SOT-23 -> Package_TO_SOT_SMD:SOT-323_SC-70
- R10: value 10k -> 100k; footprint Resistor_SMD:R_0603_1608Metric -> Resistor_SMD:R_0402_1005Metric
- R21: value 0R -> 330R; footprint Resistor_SMD:R_0603_1608Metric -> Resistor_SMD:R_0402_1005Metric
- R22: value 18k -> 1M; footprint Resistor_SMD:R_0603_1608Metric -> Resistor_SMD:R_0402_1005Metric
- R23: value 10k -> 0R; footprint Resistor_SMD:R_0603_1608Metric -> Resistor_SMD:R_0402_1005Metric
- R24: value 604R -> 10k; footprint Resistor_SMD:R_0603_1608Metric -> Resistor_SMD:R_0402_1005Metric
- R25: value 10k -> 18k; footprint Resistor_SMD:R_0603_1608Metric -> Resistor_SMD:R_0402_1005Metric
- R26: footprint Resistor_SMD:R_0603_1608Metric -> Resistor_SMD:R_0402_1005Metric
- R27: value 5.1k -> 604R; footprint Resistor_SMD:R_0603_1608Metric -> Resistor_SMD:R_0402_1005Metric
- R28: value 2.2M -> 10k; footprint Resistor_SMD:R_0603_1608Metric -> Resistor_SMD:R_0402_1005Metric
- R6: value 0R -> 100k; footprint Resistor_SMD:R_0603_1608Metric -> Resistor_SMD:R_0402_1005Metric
- R7: value 5.1k -> 10k; footprint Resistor_SMD:R_0603_1608Metric -> Resistor_SMD:R_0402_1005Metric
- U2: value BQ25185DLHR -> SN74LVC2G126DCUR; footprint pager-carrier:BQ25185_WSON-10_DLH0010A_2.2x2mm_P0.4mm_EP0.9x1.5mm -> Package_SO:VSSOP-8_2.3x2mm_P0.5mm
- U4: value TPS62840DLCR -> LIS2DW12TR; footprint pager-carrier:TPS62840_VSON-HR-8_DLC0008B_1.5x2mm_P0.5mm -> Package_LGA:LGA-12_2x2mm_P0.5mm
- moved R21 132.4 mm to (119.7, 96.6), turned to 90 degrees
- moved C19 106.6 mm to (104.3, 70.2), turned to 90 degrees
- moved C10 105.1 mm to (119.2, 76.0), turned to 180 degrees
- moved R22 103.2 mm to (120.9, 85.1)
- moved R10 90.4 mm to (102.2, 89.5), turned to -90 degrees
- moved C2 77.6 mm to (82.7, 64.5), turned to 180 degrees
- moved C18 75.2 mm to (85.4, 77.0)
- moved C17 70.5 mm to (120.0, 67.7), turned to -90 degrees
- moved R6 69.1 mm to (90.1, 63.4), turned to 90 degrees
- moved R26 66.6 mm to (111.2, 24.2)
- moved R7 66.3 mm to (88.5, 68.7)
- moved R28 65.4 mm to (111.2, 28.2)
- moved C9 62.3 mm to (91.7, 63.1), turned to 180 degrees
- moved C15 59.2 mm to (115.2, 26.4)
- moved R24 54.0 mm to (108.3, 36.1)
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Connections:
- C10 pad 1: Net-(Q2-G) -> 3V3_AWK
- C10 pad 2: SYS -> GND
- C15 pad 1: SYS_SW -> SYS
- C16 pad 1: SYS_SW -> VBAT
- C17 pad 1: SYS_SW -> VBAT
- C18 pad 1: SYS -> VBUS_DET
- C19 pad 1: VBAT -> SYS_SW
- C2 pad 1: VBUS_DET -> VBUS
- C9 pad 1: Net-(U2-IN) -> /Core/BRG_3V3
- J5 pad 2: GND -> Net-(J5-Pin_2)
- Q2 pad 2: SYS -> Net-(Q2-S)
- Q2 pad 3: SYS_SW -> /Core/FL_N
- R10 pad 1: Net-(U2-TS/MR) -> Net-(Q2-G)
- R21 pad 1: 3V3 -> /Core/EXT_LED
- R21 pad 2: Net-(J5-Pin_1) -> Net-(J4-Pin_1)
- R22 pad 1: Net-(U2-ILIM/VSET) -> Net-(J5-Pin_2)
- R22 pad 2: GND -> Net-(J5-Pin_1)
- R23 pad 1: 3V3 -> VBUS
- R23 pad 2: CHG_STAT1 -> Net-(U5-IN)
- R24 pad 1: Net-(U2-ISET) -> Net-(U5-TS/MR)
- R25 pad 1: 3V3 -> Net-(U5-ILIM/VSET)
- R25 pad 2: CHG_STAT2 -> GND
- R26 pad 1: Net-(SW4-B) -> 3V3
- R26 pad 2: Net-(Q2-G) -> CHG_STAT1
- R28 pad 1: Net-(Q2-G) -> 3V3
- R28 pad 2: SYS -> CHG_STAT2
- R6 pad 1: VBUS -> Net-(Q1B-E2)
- R6 pad 2: Net-(U2-IN) -> GND
- R7 pad 1: Net-(J13-CC2) -> Net-(Q1B-E2)
- R7 pad 2: GND -> Net-(Q1A-B1)
- U2 pad 1: SYS -> VBUS_DET
- U2 pad 2: VBAT -> /Core/ESP_TX0
- U2 pad 3: CHG_STAT2 -> /Core/ESP_RX0
- U2 pad 5: GND -> /Core/BRG_TXD
- U2 pad 6: Net-(U2-TS/MR) -> /Core/BRG_RXD
- U2 pad 7: Net-(U2-ILIM/VSET) -> VBUS_DET
- U2 pad 8: Net-(U2-ISET) -> /Core/BRG_3V3
- U4 pad 1: GND -> AON_SCL
- U4 pad 2: SYS_SW -> 3V3
- U4 pad 3: Net-(U4-MODE) -> GND
- U4 pad 4: Net-(U4-EN) -> AON_SDA
- U4 pad 5: Net-(U4-VSET) -> unconnected-(U4-NC-Pad5)
- U4 pad 7: Net-(U4-SW) -> GND
- U4 pad 8: 3V3 -> GND
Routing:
- net 3V3_AWK: track 0.00 -> 29.4 mm
- net /Core/ACC_INT1: track 0.00 -> 14.3 mm
- net VBAT: track 0.00 -> 13.3 mm
- net VBUS: track 0.00 -> 13.0 mm
- net SYS_SW: track 0.00 -> 10.4 mm
- net Net-(Q2-G): track 0.00 -> 9.15 mm
- net 3V3: track 0.00 -> 8.89 mm
- net /Core/FL_P: track 0.00 -> 8.48 mm
- net Net-(J5-Pin_1): track 0.00 -> 7.74 mm
- net Net-(Q2-S): track 0.00 -> 7.74 mm
- net GND: track 0.00 -> 6.99 mm, vias 0 -> 2
- net /Core/BRG_3V3: track 0.32 -> 7.01 mm
- net Net-(J5-Pin_2): track 0.00 -> 6.42 mm
- net Net-(U7-SW): track 0.00 -> 6.20 mm
- net AON_SDA: track 0.00 -> 5.98 mm
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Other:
- board outline added: 62.8 x 46 mm
- board text added: "BATT"
- board text added: "Haptic"
- board text added: "KBD"
- board text added: "LED"
- board text added: "Piezo"
- board text added: "USB"
